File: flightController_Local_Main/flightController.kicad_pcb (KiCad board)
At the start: 2 copper layers, 14 parts, among them J1 U.FL-R-SMT10, J2 Conn_ARM_JTAG_SWD_10, J2 Conn_ARM_SWD, J3 1054500101, U1 TPS562201DDCR, U2 TESEO-LIV3F, U3 DPS368XTSA1, U4 STM32H723VETx

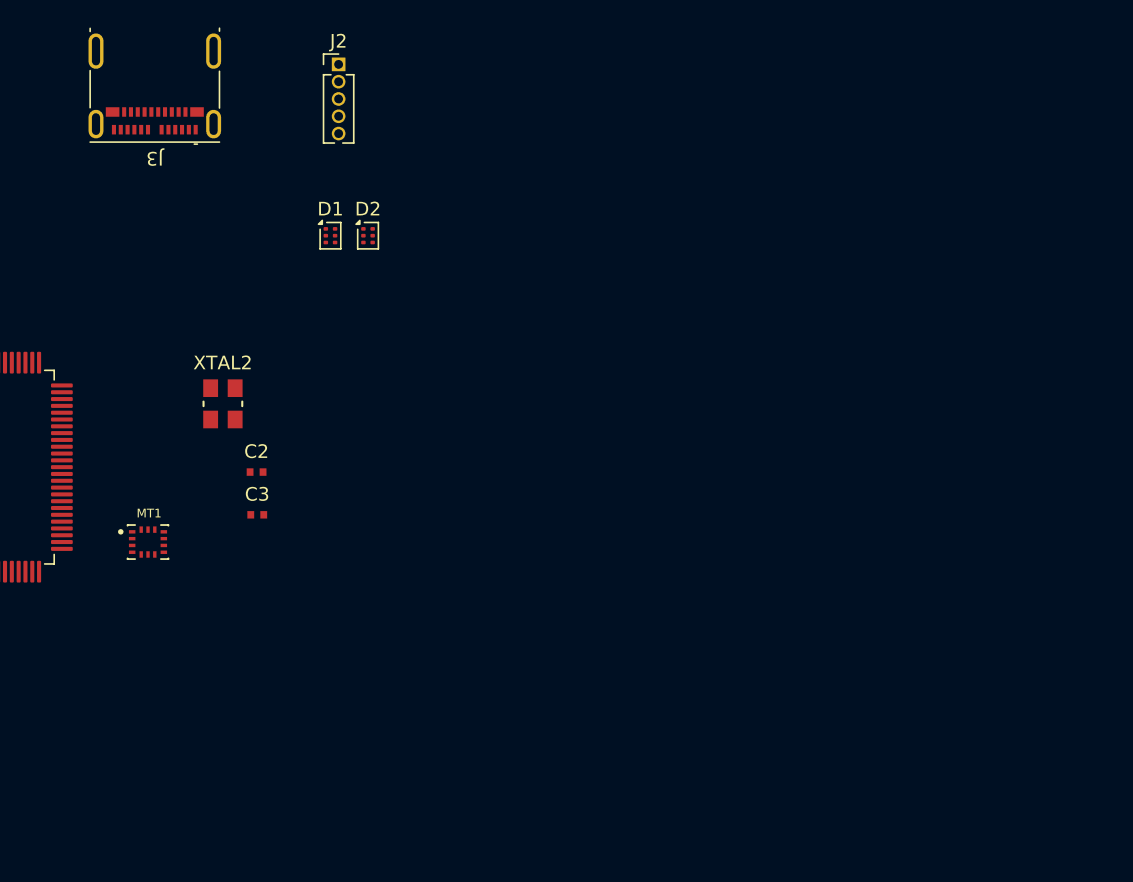
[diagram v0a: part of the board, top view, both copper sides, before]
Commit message: adding footprints and models for buck
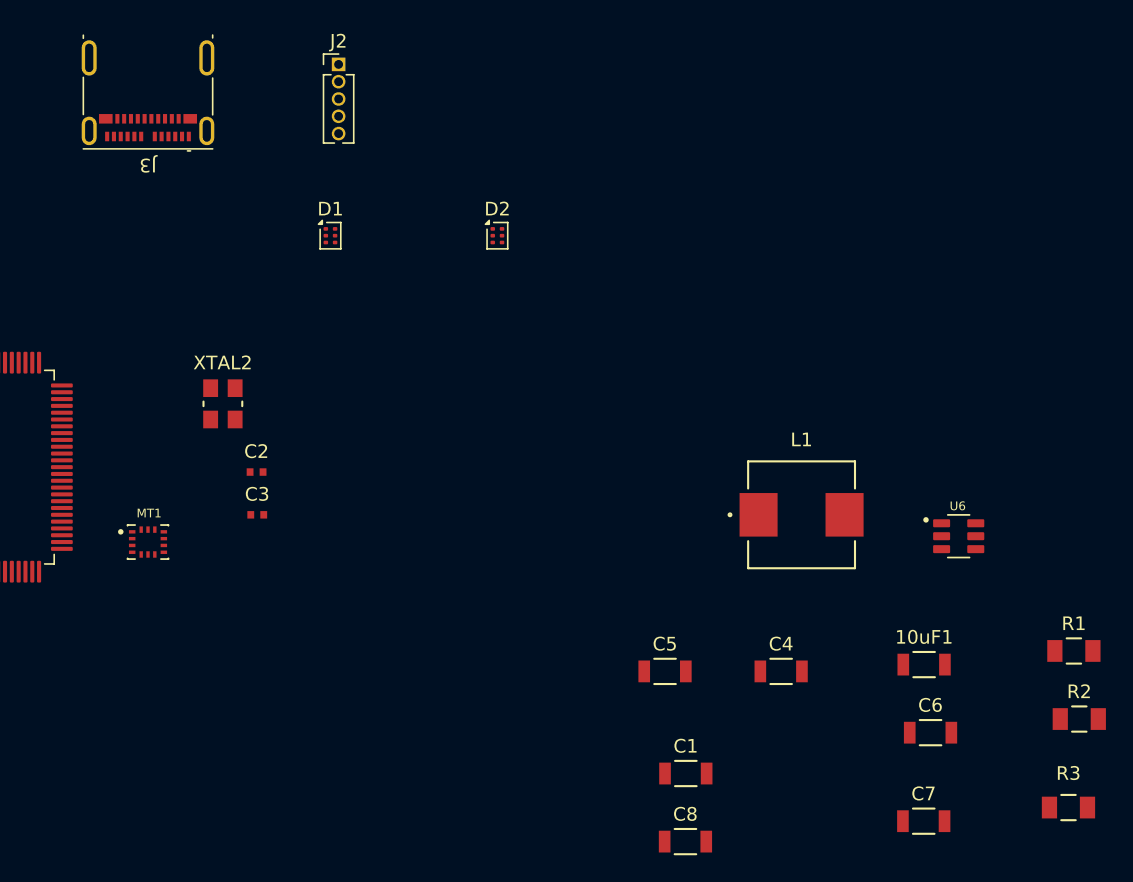
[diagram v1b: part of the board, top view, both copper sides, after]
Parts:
- added 10uF1: C9, Library:10uF_cap, F.Cu at (194.0, 106.5)
- added C1: 0.1uF, Library:01uF_CAP, F.Cu at (176.5, 114.5)
- added C4: 22uF, Library:22Uf_CAP, F.Cu at (183.5, 107.0)
- added C5: 22uF, Library:22Uf_CAP, F.Cu at (175.0, 107.0)
- added C6: 10uF, Library:10uF_cap, F.Cu at (194.5, 111.5)
- added C7: 10uF, Library:10uF_cap, F.Cu at (194.0, 118.0)
- added C8: 0.1uF, Library:01uF_CAP, F.Cu at (176.5, 119.5)
- added L1: 3.3uH, Library:3_3_Inductor, F.Cu at (185.0, 95.5)
- added R1: 10k, Library:10kResistor, F.Cu at (205.0, 105.5)
- added R2: 10k, Library:10kResistor, F.Cu at (205.4, 110.5)
- added R3: 33.2k, Library:33.2Resistor, F.Cu at (204.6, 117.0)
- added U6: TPS562201DDCR, Library:3.3Buck, F.Cu at (196.5, 97.1)
- moved D2 9.50 mm to (162.7, 75.0)
- moved J3 0.71 mm to (137.0, 64.5)
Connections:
- J2 pad 1: +3.3V_USB -> +3.3V
- J2 pad 3: SWDIO -> unconnected-(J2-SWDIO-Pad3)
- J2 pad 5: NRST -> unconnected-(J2-~{RESET}-Pad5)
- MT1 pad 5: +3.3V_Flight -> /3.3V
- MT1 pad 8: +3.3V_Flight -> /3.3V
- U4 pad 14: NRST -> unconnected-(U4-NRST-Pad14)
- U4 pad 72: SWDIO -> unconnected-(U4-PA13(JTMS-Pad72)

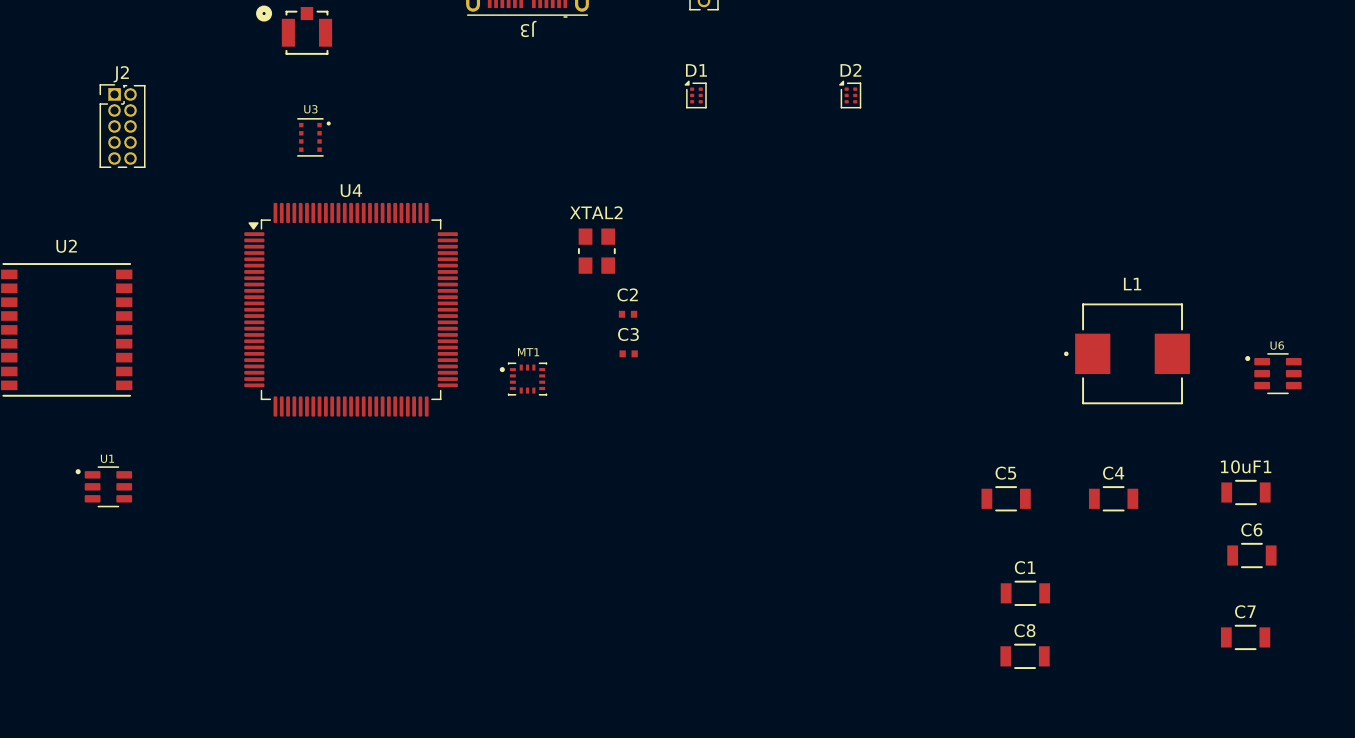
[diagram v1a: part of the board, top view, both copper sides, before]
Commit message: Adding caps to IMU and Barometer
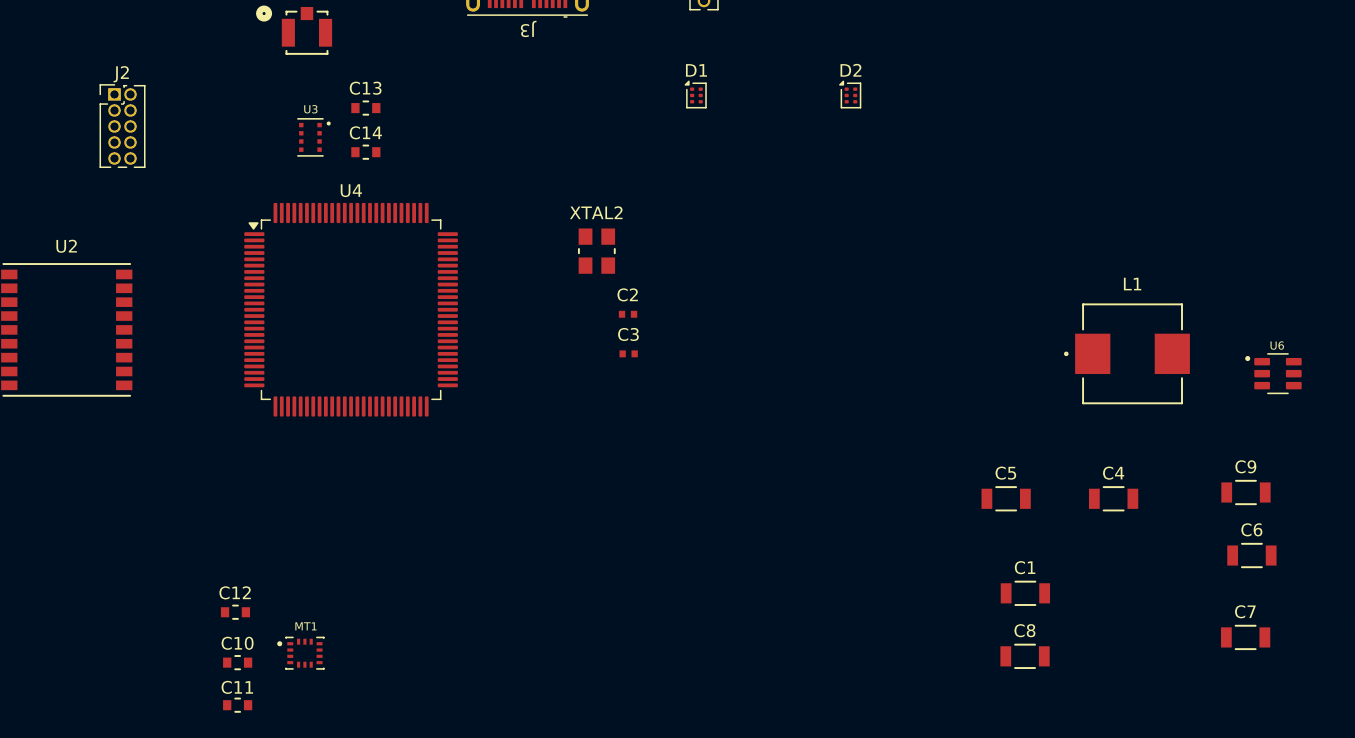
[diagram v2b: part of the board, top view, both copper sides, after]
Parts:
- removed U1: TPS562201DDCR, Library:3.3Buck
- added C10: 2.2uF, Library:2.2uF_CAP_0603, F.Cu at (114.0, 120.0)
- added C11: 0.1uF, Library:01uF_Cap_0603, F.Cu at (114.0, 123.4)
- added C12: 10nF, Library:01uF_Cap_0603, F.Cu at (113.8, 116.0)
- added C13: 0.1uF, Library:01uF_Cap_0603, F.Cu at (124.2, 76.0)
- added C14: 0.1uF, Library:01uF_Cap_0603, F.Cu at (124.2, 79.5)
- C9: renamed from 10uF1; value C9 -> 10uF
- J3: value 1054500101 -> USBC
- moved MT1 28.0 mm to (119.3, 119.2)
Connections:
- C4 pad 1: Net-(C4-Pad1) -> +3.3V
- C5 pad 1: Net-(C4-Pad1) -> +3.3V
- L1 pad 1: Net-(C4-Pad1) -> +3.3V
- MT1 pad 5: /3.3V -> +3.3V
- MT1 pad 8: /3.3V -> +3.3V
- R1 pad 2: EN -> +9V
- U2 pad 1: GND -> unconnected-(U2-GND-Pad1)
- U2 pad 10: GND_RF -> unconnected-(U2-GND_RF-Pad10)
- U2 pad 12: GND_RF -> unconnected-(U2-GND_RF-Pad12)
- U2 pad 2: TX -> GND
- U2 pad 3: RX -> TX
- U2 pad 4: PPS -> RX
- U2 pad 5: WAKE_UP -> PPS
- U2 pad 8: /3.3V -> SYS_RSTN
- U2 pad 9: SYS_RSTN -> WAKE_UP
- U3 pad 1: GND -> GND1
- U3 pad 6: /3.3V -> +3.3V
- U3 pad 7: GND -> GND1
- U3 pad 8: /3.3V -> +3.3V

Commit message: Adding updates
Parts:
- removed D2: ESD9B3.3ST5G, Package_TO_SOT_SMD:SOT-886
- removed the J2 at (151.0, 62.4)
- removed the J2 at (104.2, 74.9)
- added J2: Conn_ARM_SWD, Connector_PinHeader_1.27mm:PinHeader_1x05_P1.27mm_Vertical, F.Cu at (150.5, 99.1)
- D1: value ESD9B3.3ST5G -> ESD Protection; footprint Package_TO_SOT_SMD:SOT-886 -> Library:ESD_6V (3)
- moved R2 85.8 mm to (119.7, 115.9)
- moved R1 85.6 mm to (119.7, 112.7)
- moved R3 84.9 mm to (119.7, 119.2)
- moved C7 75.7 mm to (119.7, 102.9)
- moved C6 75.7 mm to (119.7, 99.6)
- moved C9 74.3 mm to (119.7, 109.4)
- moved C4 65.2 mm to (119.7, 93.1)
- moved C1 61.9 mm to (119.7, 89.9)
- moved U6 58.3 mm to (142.7, 119.4)
- moved C8 58.3 mm to (119.7, 106.2)
- moved C5 56.2 mm to (119.7, 96.4)
- moved D1 49.2 mm to (123.2, 116.0)
- moved J3 47.9 mm to (145.4, 111.7), turned to 0 degrees
- moved U3 43.3 mm to (129.3, 120.6)
- moved J1 42.9 mm to (145.6, 104.1)
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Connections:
- D1 pad 1: GND -> unconnected-(D1-A1-Pad1)
- D1 pad 2: SWDIO -> unconnected-(D1-A2-Pad2)
- J3 pad A1: unconnected-(J3-PadA1) -> GND1
- J3 pad A4: unconnected-(J3-PadA4) -> VBUS
- J3 pad A5: unconnected-(J3-PadA5) -> Net-(J3-PadA5)
- J3 pad A6: unconnected-(J3-PadA6) -> D+
- J3 pad A7: unconnected-(J3-PadA7) -> D-
- J3 pad A9: unconnected-(J3-PadA9) -> VBUS
- J3 pad B1: unconnected-(J3-PadB1) -> GND1
- J3 pad B12: unconnected-(J3-PadB12) -> GND1
- J3 pad B4: unconnected-(J3-PadB4) -> VBUS
- J3 pad B5: unconnected-(J3-PadB5) -> Net-(J3-PadB5)
- J3 pad B6: unconnected-(J3-PadB6) -> D+
- J3 pad B7: unconnected-(J3-PadB7) -> D-
- J3 pad B9: unconnected-(J3-PadB9) -> VBUS
- U2 pad 1: unconnected-(U2-GND-Pad1) -> GND1
- U2 pad 10: unconnected-(U2-GND_RF-Pad10) -> GND1
- U2 pad 12: unconnected-(U2-GND_RF-Pad12) -> GND1
- U2 pad 14: /3.3V -> unconnected-(U2-VCC_RF-Pad14)
- U2 pad 2: GND -> TX
- U2 pad 3: TX -> RX
- U2 pad 4: RX -> PPS
- U2 pad 5: PPS -> WAKE_UP
- U2 pad 6: /3.3V -> +3.3V
- U2 pad 7: /3.3V -> +3.3V
- U2 pad 8: SYS_RSTN -> +3.3V
- U2 pad 9: WAKE_UP -> SYS_RSTN
- U4 pad 14: unconnected-(U4-NRST-Pad14) -> NRST
- U4 pad 45: unconnected-(U4-PE15-Pad45) -> ANT_FAULT
- U4 pad 72: unconnected-(U4-PA13(JTMS-Pad72) -> SWDIO

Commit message: Adding all step files and footprints
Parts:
- added C15: 100nF, Capacitor_SMD:C_0603_1608Metric, F.Cu at (80.2, 61.5)
- added C16: 1nF, Capacitor_SMD:C_0603_1608Metric, F.Cu at (80.2, 64.0)
- added C17: 1uF, Capacitor_SMD:C_0603_1608Metric, F.Cu at (74.5, 76.0)
- added C18: 0.1uF, Capacitor_SMD:C_0603_1608Metric, F.Cu at (24.4, 64.0)
- added C19: 4.7uF, Capacitor_SMD:C_0603_1608Metric, F.Cu at (24.4, 66.5)
- added C20: 1uF, Capacitor_SMD:C_0603_1608Metric, F.Cu at (35.7, 67.7)
- added C21: 4.7uF, Capacitor_SMD:C_0603_1608Metric, F.Cu at (42.1, 73.5)
- added C22: 220nF, Capacitor_SMD:C_0603_1608Metric, F.Cu at (90.5, 59.5)
- added C23: 0.1uF, Capacitor_SMD:C_0603_1608Metric, F.Cu at (90.5, 62.0)
- added C24: 10nF, Capacitor_SMD:C_0603_1608Metric, F.Cu at (111.1, 78.9)
- added C25: 0.1uF, Capacitor_SMD:C_0603_1608Metric, F.Cu at (90.5, 64.5)
- added C26: 10uF, Capacitor_SMD:C_1206_3216Metric, F.Cu at (95.3, 59.9)
- added C27: 0.1uF, Capacitor_SMD:C_0603_1608Metric, F.Cu at (111.1, 81.4)
- added C28: 0.8pF, Capacitor_SMD:C_0603_1608Metric, F.Cu at (111.1, 84.0)
- added C29: 1.2pF, Capacitor_SMD:C_0603_1608Metric, F.Cu at (111.1, 86.5)
- added C30: 1.2pF, Capacitor_SMD:C_0603_1608Metric, F.Cu at (111.1, 89.0)
- added C31: 0.5pF, Capacitor_SMD:C_0603_1608Metric, F.Cu at (115.2, 91.5)
- added C32: 100pF, Capacitor_SMD:C_0603_1608Metric, F.Cu at (115.1, 78.9)
- added C33: 0.1uF, Capacitor_SMD:C_0603_1608Metric, F.Cu at (115.1, 81.4)
- added C34: 10nF, Capacitor_SMD:C_0603_1608Metric, F.Cu at (115.1, 84.0)
- added C35: 470nF, Capacitor_SMD:C_0603_1608Metric, F.Cu at (115.1, 86.5)
- added C36: 22uF, Capacitor_SMD:C_0805_2012Metric, F.Cu at (67.5, 21.0)
- added C37: 22uF, Capacitor_SMD:C_0805_2012Metric, F.Cu at (67.5, 24.0)
- added C38: 10uF, Capacitor_SMD:C_1206_3216Metric, F.Cu at (73.5, 21.0)
- added C39: 10uF, Capacitor_SMD:C_1206_3216Metric, F.Cu at (73.5, 25.5)
- added C40: 0.1uF, Capacitor_SMD:C_0603_1608Metric, F.Cu at (73.0, 29.5)
- added C41: 0.1uF, Capacitor_SMD:C_0603_1608Metric, F.Cu at (73.2, 32.5)
- added C42: 10uF, Capacitor_SMD:C_0805_2012Metric, F.Cu at (68.0, 36.0)
- added D2: ESD Protection, Library:ESD_6V (3), F.Cu at (17.3, 54.0)
- added J4: U.FL-R-SMT10, Library:U.FL_CONN_v.UL, F.Cu at (104.0, 80.0)
- added J5: XT60-M, Library:XT60-M, F.Cu at (95.9, 21.0)
- added L2: 10nH, Library:10nH_Inductor, F.Cu at (73.9, 80.0)
- added L3: 3.0nH, Library:3.0nH_Inductor, F.Cu at (118.6, 78.8)
- added L4: 2.5nH, Library:3.0nH_Inductor, F.Cu at (118.6, 81.1)
- added L5: 15uH, Library:15uH_Inductor, F.Cu at (111.1, 92.0)
- added L6: 4.7uH, Library:4.7uH_7.18A, F.Cu at (56.5, 25.0)
- added M1: Motor_Servo, Connector_JST:JST_XH_B3B-XH-AM_1x03_P2.50mm_Vertical, F.Cu at (87.0, 31.5)
- added M2: Motor_Servo, Connector_JST:JST_XH_B3B-XH-AM_1x03_P2.50mm_Vertical, F.Cu at (100.0, 31.5)
- added R10: 0, Resistor_SMD:R_0603_1608Metric, F.Cu at (115.1, 89.0)
- added R11: 10k, Resistor_SMD:R_0603_1608Metric, F.Cu at (67.7, 28.7)
- added R12: 10k, Resistor_SMD:R_0603_1608Metric, F.Cu at (67.7, 32.0)
- added R13: 68.1k, Resistor_SMD:R_0603_1608Metric, F.Cu at (73.5, 36.0)
- added R4: 10k, Resistor_SMD:R_0603_1608Metric, F.Cu at (80.2, 66.5)
- added R5: 100k, Resistor_SMD:R_0603_1608Metric, F.Cu at (36.2, 73.0)
- added R6: 5.1k, Resistor_SMD:R_0603_1608Metric, F.Cu at (17.5, 57.0)
- added R7: 5.1k, Resistor_SMD:R_0603_1608Metric, F.Cu at (17.5, 59.5)
- added R8: 75k, Resistor_SMD:R_0603_1608Metric, F.Cu at (24.4, 71.5)
- added R9: 100k, Resistor_SMD:R_0603_1608Metric, F.Cu at (42.1, 76.0)
- added U1: BD33IA5WEFJ-E2, Library:3.3V-LDO (2), F.Cu at (42.7, 65.4)
- added U10: SX1281IMLTRT, Library:XCVR_SX1281IMLTRT, F.Cu at (97.5, 80.0)
- added U11: LIS2MDLTR, Library:Magnetometer, F.Cu at (86.3, 59.9)
- added U12: TPS562201DDCR, Library:3.3Buck, F.Cu at (61.5, 35.0)
- added U5: TPS22944DCKR, Library:TPS22944 (2), F.Cu at (75.2, 71.6)
- added U7: MIC2004-0.5YM5-TR, Library:Current-Limiter-500mA (1), F.Cu at (29.3, 67.5)
- added U8: LM66100DCKR, Library:Ideal_diode (2), F.Cu at (52.5, 65.1)
- added U9: LM66100DCKR, Library:Ideal_diode (2), F.Cu at (52.4, 73.0)
- added XTAL1: NX2016SA-52MHZ-EXS00A-CS07103, Library:Tranny_OSC, F.Cu at (102.9, 86.3)
- C1, C8: footprint Library:01uF_CAP -> Capacitor_SMD:C_0603_1608Metric
- C10: footprint Library:2.2uF_CAP_0603 -> Capacitor_SMD:C_0603_1608Metric
- C11, C12, C13, C14: footprint Library:01uF_Cap_0603 -> Capacitor_SMD:C_0603_1608Metric
- C2, C3: footprint Library:0.22Cap -> Capacitor_SMD:C_0603_1608Metric
- C4, C5: footprint Library:22Uf_CAP -> Capacitor_SMD:C_0805_2012Metric
- C6, C7: footprint Library:10uF_cap -> Capacitor_SMD:C_1206_3216Metric
- C9: footprint Library:10uF_cap -> Capacitor_SMD:C_0805_2012Metric
- L1: footprint Library:3_3_Inductor -> Library:3.3uH_3.94A
- R1, R2: footprint Library:10kResistor -> Resistor_SMD:R_0603_1608Metric
- R3: footprint Library:33.2Resistor -> Resistor_SMD:R_0603_1608Metric
- moved U6 144.4 mm to (25.5, 35.0)
- moved L1 137.5 mm to (26.0, 27.5)
- moved J3 132.8 mm to (26.0, 53.5)
- moved D1 124.2 mm to (17.3, 51.0)
- moved R2 118.8 mm to (30.5, 37.5)
- moved R3 118.8 mm to (30.3, 41.0)
- moved C8 114.8 mm to (30.5, 34.0)
- moved C6 112.6 mm to (34.5, 26.0)
- moved C7 112.1 mm to (34.5, 30.0)
- moved C9 110.4 mm to (30.4, 44.5)
- moved R1 109.0 mm to (34.7, 44.5)
- moved C4 103.7 mm to (34.5, 34.0)
- moved C5 103.5 mm to (34.6, 37.5)
- moved C1 98.1 mm to (34.7, 41.0)
- moved U4 92.5 mm to (52.0, 50.7)
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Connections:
- net +9V renamed +15V
- net AP_CS renamed SPI_2_NSS_IMU
- net AP_SCLK renamed SPI_2_SCK_IMU
- net AP_SDA renamed SPI_2_MISO_IMU
- net AP_SDO renamed SPI_2_MOSI_IMU
- C4 pad 1: +3.3V -> +3.3V_Batt
- C5 pad 1: +3.3V -> +3.3V_Batt
- C9 pad 2: +3.3V -> +3.3V_Batt
- D1 pad 1: unconnected-(D1-A1-Pad1) -> D+
- D1 pad 2: unconnected-(D1-A2-Pad2) -> Net-(D1-A2)
- J3 pad A4: VBUS -> +5V_VBUS
- J3 pad A6: D+ -> Net-(D1-A2)
- J3 pad A7: D- -> Net-(D2-A2)
- J3 pad A9: VBUS -> +5V_VBUS
- J3 pad B4: VBUS -> +5V_VBUS
- J3 pad B6: D+ -> Net-(D1-A2)
- J3 pad B7: D- -> Net-(D2-A2)
- J3 pad B9: VBUS -> +5V_VBUS
- L1 pad 1: +3.3V -> +3.3V_Batt
- R3 pad 1: +3.3V -> +3.3V_Batt
- U3 pad 2: CSB -> SPI_4_NSS_Baro
- U3 pad 3: SDA -> SPI_4_MISO
- U3 pad 4: SCK -> SPI_4_SCK
- U3 pad 5: SDO -> SPI_4_MOSI
- U4 pad 1: unconnected-(U4-PE2-Pad1) -> SPI_4_SCK
- U4 pad 2: unconnected-(U4-PE3-Pad2) -> SPI_4_CS_MAG
- U4 pad 3: unconnected-(U4-PE4-Pad3) -> SPI_4_NSS_Baro
- U4 pad 36: unconnected-(U4-PB2-Pad36) -> RF_Transciever_RESET
- U4 pad 4: unconnected-(U4-PE5-Pad4) -> SPI_4_MISO
- U4 pad 5: unconnected-(U4-PE6-Pad5) -> SPI_4_MOSI
- U4 pad 63: unconnected-(U4-PC6-Pad63) -> TIM3_CH1_PWM
- U4 pad 64: unconnected-(U4-PC7-Pad64) -> TIM3_CH2_PWM
- U4 pad 68: unconnected-(U4-PA9-Pad68) -> +5V_VBUS
- U4 pad 70: unconnected-(U4-PA11-Pad70) -> D-
- U4 pad 71: unconnected-(U4-PA12-Pad71) -> D+
- U4 pad 77: CSB -> SPI_1_NSS_Transciever
- U4 pad 83: unconnected-(U4-PD2-Pad83) -> DIO1_EXTI
- U4 pad 84: unconnected-(U4-PD3-Pad84) -> DIO2_EXTI
- U4 pad 85: unconnected-(U4-PD4-Pad85) -> DIO3_EXTI
- U4 pad 86: unconnected-(U4-PD5-Pad86) -> BUSY
- U4 pad 89: SCK -> SPI_1_SCK_Transciever
- U4 pad 90: SDA -> SPI_1_MISO_Transciever
- U4 pad 91: SDO -> SPI_1_MOSI_Transciever
